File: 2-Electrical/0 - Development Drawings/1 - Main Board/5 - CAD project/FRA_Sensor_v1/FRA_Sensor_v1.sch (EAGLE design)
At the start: 140 parts, among them IC1 CP2101, IC2 LMV611, IC3 TS520533, J2 ETH_CONN, J3 USB, Q1 Si2300DS, Q2 FDN306P, T1 BC847, T2 BC847, T3 BC847, U2 ESP-WROOM-32, Y3 32.768kHz

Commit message: sch
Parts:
- removed C21, C22: 10u, resistor:C-EUC0603K
- removed C23: 220u, resistor:CPOL-EU153CLV-0605
- removed C31: 100n, resistor:C-EUC0603K
- removed C8: DNI, resistor:C-EUC0603K
- removed L1: 2.2uH, resistor:L-EUL3225M
- removed LIGHT_DR: LDR, pinhead:PINHD-1X2
- removed R20: 1G, resistor:R-EU_R0603
- removed R26: 0, resistor:R-EU_R0603
- removed R27: DNI, resistor:R-EU_R0603
- removed R41, R45, R46: 12k, resistor:R-EU_R0603
- removed TP13, TP28, TP29, TP30: TPTP10R, testpad:TPTP10R
- added D4, D6: PESD1CAN, diode:PESD1CAN
- added D7, D8: (no value), SparkFun-LED:LED5MM
- added J1: (no value), con-jack:JACK-PLUG1
- added LIGHT_DR1: LDR, pinhead:PINHD-1X2
- added R68, R69: 10K, resistor:R-EU_R0603
- added S1, S2: (no value), adafruit:31-XX
- added TP1, TP2, TP3, TP4: TPTP10R, testpad:TPTP10R
- added U$5, U$6: MOUNTINGHOLE3.0THIN, microbuilder:MOUNTINGHOLE3.0THIN
- added X1: TB001-500-02BE, con-wago-500:W237-102
- C10, C17: value 10u -> DNI
- C29, C30: value 22p(DNI) -> 22p
- C7: value DNI -> 220u; device resistor:C-EUC0603K -> resistor:CPOL-EU153CLV-0605
- R14: value 220k -> 100
- R15: value 100k -> 100
- R18: value 2M7 -> 100
- R19: value 47k -> 100
- R53, R54: value 10k -> 100k
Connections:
- net N$12 renamed P_RTC
- net N$13 renamed N_RTC
- removed net ADC: C31.2, R14.2, R15.2
- removed net N$14: LIGHT_DR.2, R14.1, R18.1, R19.2, R20.1
- removed net N$16: D3.A
- removed net N$27: R41.1
- removed net N$37: L1.1
- removed net N$40: R45.2, R46.1
- removed net N$9: C7.1, C8.2, R26.2, R27.1
- new net BTN1: R68.1, S1.P, U2.IO2
- new net BTN2: R69.1, S2.P, U2.IO4
- new net LED: R18.2, R19.2, U2.IO16
- new net N$6: D8.A, R18.1, R19.1
- new net N$7: D7.A, R14.1, R15.1
- net 3.3V: now also D6.3, R14.2, R15.2, R68.2, R69.2, TP2.TP; no longer C21.1, C23.+, C8.1, L1.2, LIGHT_DR.1, R18.2, R20.2, R26.1, R46.2, TP11.TP
- net 5V: now also TP3.TP; no longer C22.1, R41.2, TP28.TP, TP29.TP
- net GND: now also C7.-, D4.1, D4.2, D6.1, D6.2, D7.C, D8.C, J1.1, J1.2, S1.S, S2.S, X1-2.KL; no longer C21.2, C22.2, C23.-, C31.1, C7.2, R15.1, R19.1, R27.2, R45.1, TP13.TP, TP30.TP
- net N$22: now also TP4.TP
- net N$23: now also TP1.TP
- net N$35: no longer C20.2
- net NRST: now also JTAG1.10, U$2.1
- net RXD0: now also U$2.5
- net TXD0: now also U$2.3
- net VIN: now also D4.3, J1.3, X1-1.KL
- net VIN_PROTECTED: now also C7.+, TP11.TP
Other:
- note added: "6-12V"
- note added: "Vin max 17V"
- note removed: "Ambient Light Sensor"

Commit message: dev and sd
mac address changed
other sample testing
sd card example setup
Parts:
- added U$7: ETH_MODULE_OUTLINE, FRA_eagle_lib:ETH_MODULE_OUTLINE
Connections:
- new net ETH_5V: J2.12
- new net ETH_CLKOUT: J2.9
- new net ETH_INT: J2.10
- new net ETH_RST: J2.4
- new net ETH_WOL: J2.7
- net 3.3V: now also C39.1, C40.1, J2.2
- net BTN1: no longer U2.IO2
- net BTN2: no longer U2.IO4
- net GND: now also J2.1, J2.11
- net SD_CS_MCU: now also U2.IO17; no longer U2.IO25
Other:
- note added: "female"
- note added: "place on BOT"

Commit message: placment drafts
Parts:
- added SENSOR_10, SENSOR_2, SENSOR_3, SENSOR_4, SENSOR_5, SENSOR_6, SENSOR_7, SENSOR_8, SENSOR_9: SENS1, pinhead:PINHD-1X4
- SENSOR_1: value LED_ring_12 -> SENS1
- renumbered LED_12 to SENSOR_1
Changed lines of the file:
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@@
 <part name="R21" library="resistor" deviceset="R-EU_" device="R0603" value="0"/>
 <part name="D3" library="nxp_60" deviceset="BAS17" device=""/>
-<part name="LED_12" library="pinhead" deviceset="PINHD-1X4" device="" value="LED_ring_12"/>
+<part name="SENSOR_1" library="pinhead" deviceset="PINHD-1X4" device="" value="SENS1"/>
 <part name="R25" library="resistor" deviceset="R-EU_" device="R0603" value="10K"/>
 <part name="C16" library="resistor" deviceset="C-EU" device="C0603K" value="1n"/>
@@
 <part name="SUPPLY54" library="supply2" deviceset="GND" device=""/>
 <part name="U$7" library="FRA_eagle_lib" deviceset="ETH_MODULE_OUTLINE" device=""/>
+<part name="SENSOR_2" library="pinhead" deviceset="PINHD-1X4" device="" value="SENS1"/>
+<part name="SENSOR_3" library="pinhead" deviceset="PINHD-1X4" device="" value="SENS1"/>
+<part name="SENSOR_4" library="pinhead" deviceset="PINHD-1X4" device="" value="SENS1"/>
+<part name="SENSOR_5" library="pinhead" deviceset="PINHD-1X4" device="" value="SENS1"/>
+<part name="SENSOR_6" library="pinhead" deviceset="PINHD-1X4" device="" value="SENS1"/>
+<part name="SENSOR_7" library="pinhead" deviceset="PINHD-1X4" device="" value="SENS1"/>
+<part name="SENSOR_8" library="pinhead" deviceset="PINHD-1X4" device="" value="SENS1"/>
+<part name="SENSOR_9" library="pinhead" deviceset="PINHD-1X4" device="" value="SENS1"/>
+<part name="SENSOR_10" library="pinhead" deviceset="PINHD-1X4" device="" value="SENS1"/>
 </parts>
 <sheets>
@@
 <instance part="SUPPLY85" gate="G$1" x="53.34" y="86.36"/>
 <instance part="D3" gate="G$1" x="30.48" y="7.62" rot="R270"/>
-<instance part="LED_12" gate="A" x="53.34" y="7.62" smashed="yes">
+<instance part="SENSOR_1" gate="A" x="53.34" y="7.62" smashed="yes">
 <attribute name="NAME" x="46.99" y="15.875" size="1.778" layer="95"/>
 </instance>
@@
 <instance part="U$6" gate="G$1" x="63.5" y="5.08"/>
 <instance part="LIGHT_DR1" gate="G$1" x="68.58" y="15.24"/>
+<instance part="SENSOR_2" gate="A" x="96.52" y="10.16" smashed="yes">
+<attribute name="NAME" x="90.17" y="18.415" size="1.778" layer="95"/>
+</instance>
+<instance part="SENSOR_3" gate="A" x="119.38" y="10.16" smashed="yes">
+<attribute name="NAME" x="113.03" y="18.415" size="1.778" layer="95"/>
+</instance>
+<instance part="SENSOR_4" gate="A" x="119.38" y="35.56" smashed="yes">
+<attribute name="NAME" x="113.03" y="43.815" size="1.778" layer="95"/>
+</instance>
+<instance part="SENSOR_5" gate="A" x="99.06" y="35.56" smashed="yes">
+<attribute name="NAME" x="92.71" y="43.815" size="1.778" layer="95"/>
+</instance>
+<instance part="SENSOR_6" gate="A" x="78.74" y="27.94" smashed="yes">
+<attribute name="NAME" x="72.39" y="36.195" size="1.778" layer="95"/>
+</instance>
+<instance part="SENSOR_7" gate="A" x="58.42" y="27.94" smashed="yes">
+<attribute name="NAME" x="52.07" y="36.195" size="1.778" layer="95"/>
+</instance>
+<instance part="SENSOR_8" gate="A" x="40.64" y="27.94" smashed="yes">
+<attribute name="NAME" x="34.29" y="36.195" size="1.778" layer="95"/>
+</instance>
+<instance part="SENSOR_9" gate="A" x="25.4" y="30.48" smashed="yes">
+<attribute name="NAME" x="19.05" y="38.735" size="1.778" layer="95"/>
+</instance>
+<instance part="SENSOR_10" gate="A" x="0" y="33.02" smashed="yes">
+<attribute name="NAME" x="-6.35" y="41.275" size="1.778" layer="95"/>
+</instance>
 </instances>
 <busses>

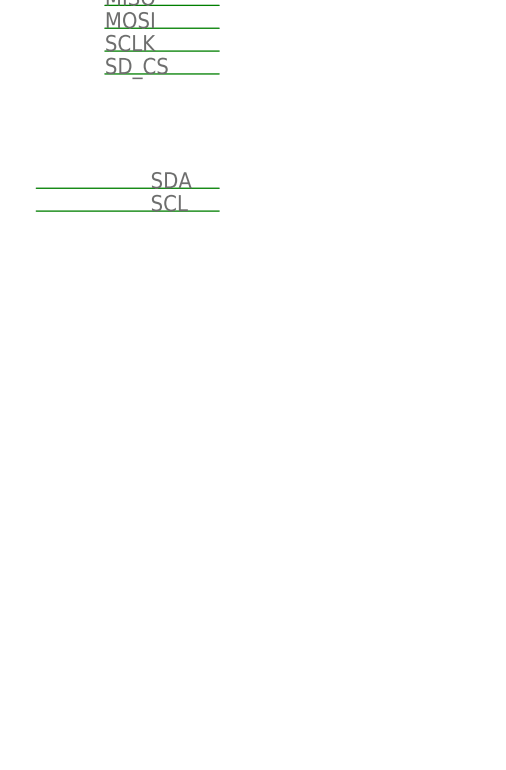
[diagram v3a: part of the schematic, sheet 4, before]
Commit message: digital sensors interface
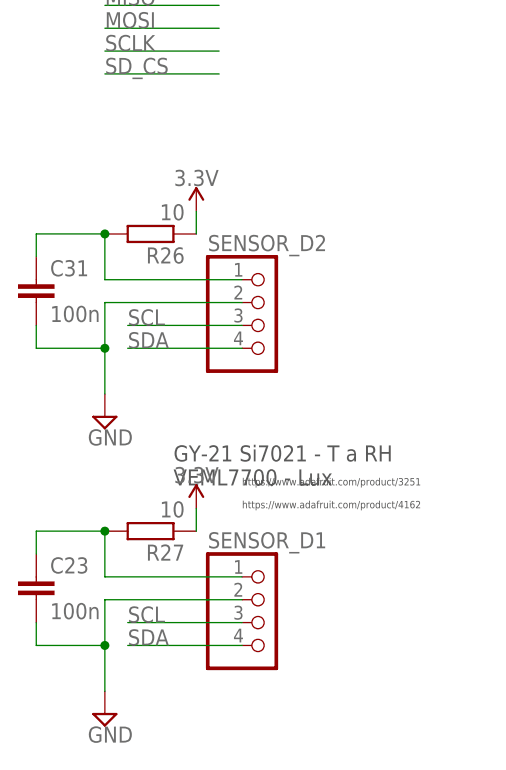
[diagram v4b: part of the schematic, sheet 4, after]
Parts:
- removed SENSOR_10, SENSOR_9: SENS1, pinhead:PINHD-1X4
- added C23, C31: 100n, resistor:C-EUC0603K
- added J5: WM9734TR-ND, SparkFun-Connectors:USB_MICRO-B_FEMALE-SMT-VERT
- added R26, R27: 10, resistor:R-EU_R0603
- added SENSOR_D1, SENSOR_D2: + G SCL SDA, pinhead:PINHD-1X4
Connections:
- new net N$4: C23.1, R27.2, SENSOR_D1.1
- new net N$5: C31.1, R26.2, SENSOR_D2.1
- net 3.3V: now also R26.1, R27.1
- net D_N: now also J5.D-
- net D_P: now also J5.D+
- net GND: now also C23.2, C31.2, J5.GND, SENSOR_D1.2, SENSOR_D2.2
- net SCL: now also SENSOR_D1.3, SENSOR_D2.3
- net SDA: now also SENSOR_D1.4, SENSOR_D2.4
- net V_USB: now also J5.VBUS
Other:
- note added: "GY-21 Si7021 - T a RH VEML7700 - Lux"
- note added: "https://www.adafruit.com/product/3251"
- note added: "https://www.adafruit.com/product/4162"
- note removed: "add ESD protection"

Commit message: sch
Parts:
- removed C37: 100n, resistor:C-EUC0603K
- removed J3: USB, SparkFun-Connectors:USB_MICRO-B_HALF_PTH_MILL
- removed R67: 10K, resistor:R-EU_R0603
- removed U$3: MICROSD, adafruit:MICROSD
- added C8: 10u, resistor:C-EUC0603K
- added FAN_5V: FAN, pinhead:PINHD-1X2
- added IC4, IC5, IC6: ADS1115BQDGSRQ1, SamacSys_Parts:ADS1115BQDGSRQ1
- added J8: 1140084168, SamacSys_Parts:1140084168
- added JP1: (no value), pinhead:PINHD-1X5
- added JP2: (no value), pinhead:PINHD-1X6
- added Q3: Si2300DS, adafruit:MOSFET-NREFLOW
- added R20: 47, resistor:R-EU_R0603
- added R41: 0(DNI), resistor:R-EU_R0603
- added R45: 0, resistor:R-EU_R0603
- added TP5: TPTP10R, testpad:TPTP10R
- R21: value 0 -> 1M
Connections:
- removed net SENSOR_DET1: C37.1, R67.1, U2.SENSOR_VP/I36
- removed net SHIELD: J3.SHIELD, R21.1
- removed net VDD: C38.1, J4.VDD, R65.1, U$3.VDD
- new net FAN: Q3.G, R20.2, R21.1, TP5.TP
- new net FAN_MCU: R20.1, U2.IO25
- new net N$10: C38.1, J4.VDD, R65.1
- new net N$8: FAN_5V.1, Q3.D
- new net N$9: D7.C, R41.1, R45.2
- net 3.3V: now also R18.2, R19.2; no longer R67.2
- net 5V: now also C8.1, FAN_5V.2
- net D_N: no longer J3.D-
- net D_P: no longer J3.D+
- net ETH_CS: now also J2.3
- net ETH_INT: now also U2.IO2
- net ETH_RST: now also U2.IO4
- net GND: now also C8.2, Q3.S, R45.1; no longer C37.2, D7.C, D8.C, J3.GND, U$3.GND, U$3.GND1, U$3.VSS
- net GPIO0: now also R41.2
- net LED: now also D8.C; no longer R18.2, R19.2
- net MISO: now also J2.8; no longer U$3.DATA_OUT
- net MOSI: now also J2.5; no longer U$3.DATA_IN
- net SCLK: now also J2.6, J4.CLK/SCLK
- net SD_CD: no longer U$3.CARD_DETECT, U$3.CARD_DETECT1
- net SD_CS: no longer U$3.CS
- net V_USB: no longer J3.VBUS
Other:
- note added: "ADDR TO GND 1b1001000 VDD 1b1001001 SDA 1b1001010 SCL 1b1001011"
- note added: "Multicomp MC34459 Mouser GSD090012SEU"
- note added: "RTC DNI"
- note added: "funnel connector and screw terminal"
- note removed: "sensor detection WIP every port???"

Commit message: sch and layiout
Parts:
- added C21: 10u, resistor:C-EUC0603K
- added FB1, FB2: (no value), microbuilder:FERRITE
- added Q4: Si2300DS, adafruit:MOSFET-NREFLOW
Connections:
- net D_N renamed D_N_
- net D_P renamed D_P_
- new net 5V1: C21.1
- new net SD_VDD: C38.1, J4.VDD, J8.SUPPLY_VOLTAGE, R65.1
- net GND: now also C21.2, J5.SHIELD, J8.CARD_DETECT_SW_1, J8.SUPPLY_VOLTAGE_GND, Q4.S
- net MISO: now also J8.DATE_LINE_[BIT_0]
- net MOSI: now also J8.COMMAND/RESPONSE
- net N$10: now also Q4.D; no longer C38.1, J4.VDD, R65.1
- net SCLK: now also J8.CLOCK
- net SD_CD: now also J8.CARD_DETECT_SW_2
- net SD_CS: now also J8.CARD_DETECT_/_DATE_LINE_[BIT_3]
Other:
- note added: "level shift needed for ADC"
- note added: "level shift needed for ADCS"
- moved on the sheet: D8, J8, R64, R65

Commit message: jtag layout
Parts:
- removed C4: 10u, resistor:C-EUC0603K
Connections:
- net 5V: no longer C4.1, C5.1
- net GND: no longer C4.2
- net V_USB: now also C5.1
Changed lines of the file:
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@@
 <part name="C2" library="resistor" deviceset="C-EU" device="C0603K" value="10u"/>
 <part name="C3" library="resistor" deviceset="C-EU" device="C0603K" value="100n"/>
-<part name="C4" library="resistor" deviceset="C-EU" device="C0603K" value="10u"/>
 <part name="C5" library="resistor" deviceset="C-EU" device="C0603K" value="100n"/>
 <part name="SUPPLY2" library="supply2" deviceset="GND" device=""/>
 <part name="SUPPLY3" library="supply2" deviceset="GND" device=""/>
-<part name="SUPPLY4" library="supply2" deviceset="GND" device=""/>
 <part name="SUPPLY5" library="supply2" deviceset="GND" device=""/>
 <part name="FRAME1" library="SparkFun-Aesthetics" deviceset="FRAME-A4L" device=""/>
@@
 <part name="SUPPLY56" library="SparkFun-PowerSymbols" deviceset="3.3V" device=""/>
 <part name="SUPPLY57" library="SparkFun-PowerSymbols" deviceset="3.3V" device=""/>
-<part name="SUPPLY58" library="SparkFun-PowerSymbols" deviceset="5V" device=""/>
-<part name="SUPPLY59" library="SparkFun-PowerSymbols" deviceset="5V" device=""/>
 <part name="SUPPLY61" library="SparkFun-PowerSymbols" deviceset="3.3V" device=""/>
 <part name="SUPPLY67" library="SparkFun-PowerSymbols" deviceset="3.3V" device=""/>
@@
 <part name="C21" library="resistor" deviceset="C-EU" device="C0603K" value="10u"/>
 <part name="SUPPLY101" library="supply2" deviceset="GND" device=""/>
+<part name="SUPPLY4" library="SparkFun-PowerSymbols" deviceset="V_USB" device=""/>
 </parts>
 <sheets>
@@
 <instance part="C2" gate="G$1" x="172.72" y="160.02"/>
 <instance part="C3" gate="G$1" x="182.88" y="160.02"/>
-<instance part="C4" gate="G$1" x="193.04" y="160.02"/>
 <instance part="C5" gate="G$1" x="203.2" y="160.02"/>
 <instance part="SUPPLY2" gate="GND" x="172.72" y="152.4"/>
 <instance part="SUPPLY3" gate="GND" x="182.88" y="152.4"/>
-<instance part="SUPPLY4" gate="GND" x="193.04" y="152.4"/>
 <instance part="SUPPLY5" gate="GND" x="203.2" y="152.4"/>
 <instance part="FRAME1" gate="G$1" x="5.08" y="2.54"/>
@@
 <instance part="SUPPLY56" gate="G$1" x="172.72" y="167.64"/>
 <instance part="SUPPLY57" gate="G$1" x="182.88" y="167.64"/>
-<instance part="SUPPLY58" gate="G$1" x="193.04" y="167.64"/>
-<instance part="SUPPLY59" gate="G$1" x="203.2" y="167.64"/>
 <instance part="SUPPLY61" gate="G$1" x="238.76" y="127"/>
 <instance part="SUPPLY67" gate="G$1" x="170.18" y="127"/>
@@
 <instance part="SUPPLY68" gate="G$1" x="88.9" y="101.6"/>
 <instance part="SUPPLY72" gate="GND" x="88.9" y="81.28"/>
+<instance part="SUPPLY4" gate="G$1" x="203.2" y="167.64"/>
 </instances>
 <busses>
@@
 </segment>
 <segment>
-<pinref part="C4" gate="G$1" pin="2"/>
-<pinref part="SUPPLY4" gate="GND" pin="GND"/>
-</segment>
-<segment>
 <pinref part="C5" gate="G$1" pin="2"/>
 <pinref part="SUPPLY5" gate="GND" pin="GND"/>
@@
 </segment>
 </net>
-<net name="5V" class="0">
-<segment>
-<pinref part="C4" gate="G$1" pin="1"/>
-<wire x1="193.04" y1="167.64" x2="193.04" y2="162.56" width="0.1524" layer="91"/>
-<pinref part="SUPPLY58" gate="G$1" pin="5V"/>
-</segment>
-<segment>
-<pinref part="C5" gate="G$1" pin="1"/>
-<wire x1="203.2" y1="167.64" x2="203.2" y2="162.56" width="0.1524" layer="91"/>
-<pinref part="SUPPLY59" gate="G$1" pin="5V"/>
-</segment>
-</net>
 <net name="V_USB" class="0">
 <segment>
@@
 <wire x1="88.9" y1="96.52" x2="88.9" y2="101.6" width="0.1524" layer="91"/>
 </segment>
-</net>
+<segment>
+<pinref part="C5" gate="G$1" pin="1"/>
+<wire x1="203.2" y1="167.64" x2="203.2" y2="162.56" width="0.1524" layer="91"/>
+<pinref part="SUPPLY4" gate="G$1" pin="V_USB"/>
+</segment>
+</net>

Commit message: power layouts
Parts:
- removed R66: 47, resistor:R-EU_R0603
- added FB3, FB4, FB5, FB6: (no value), microbuilder:FERRITE
- added Q5, Q6: Si2300DS, adafruit:MOSFET-NREFLOW
- added Q7: 100A/100V/6.8mΩ, microbuilder:MOSFET-PTO252
- added R46, R67, R70, R71: 10k, resistor:R-EU_R0603
- added TP6, TP7: TPTP10R, testpad:TPTP10R
- L2, L3: device FRA_eagle_lib:INDUCTOR -> FRA_eagle_lib:INDUCTOR6X6MM
- Q2: device microbuilder:MOSFET-NWIDE -> microbuilder:MOSFET-PWIDE
- R32, R47: value 47 -> 0
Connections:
- removed net 5V1: C21.1
- removed net ADC_CS: R66.2
- removed net ADC_CS_MCU: R66.1, U2.IO26
- removed net N$30: Q2.G, R53.1, R54.2
- new net GNDIN: FB5.P$1, FB6.P$1, J1.1, J1.2, X1-2.KL
- new net SCL_5V: Q6.D, R71.2
- new net SDA_5V: Q5.D, R67.2
- new net VGI: Q2.G, Q7.G, R53.1, R54.2
- new net VIN_IN: FB3.P$1, FB4.P$1, J1.3, X1-1.KL
- net 3.3V: now also Q5.G, Q6.G, R46.1, R70.1
- net 5V: now also R67.1, R71.1
- net GND: now also FB5.P$2, FB6.P$2; no longer J1.1, J1.2, X1-2.KL
- net SCL: now also Q6.S, R70.2, TP7.TP
- net SDA: now also Q5.S, R46.2, TP6.TP
- net VIN: now also FB3.P$2, FB4.P$2, Q2.D, Q7.D; no longer J1.3, Q2.S, R22.2, R49.2, X1-1.KL
- net VIN_PROTECTED: now also Q2.S, Q7.S, R22.2, R49.2; no longer Q2.D
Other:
- note removed: "level shift needed for ADC"
- note removed: "level shift needed for ADCS"
